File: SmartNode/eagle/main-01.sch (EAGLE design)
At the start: 151 parts, among them IC1 ATmega328P-AU, IC2 MAX3468CSA, IC4 78L33, IC5 MCP23017-E/SO-SOIC28, IC6 TPS56X200, IC7 LTC1694, Q1 IRLML2502, X0 OPI-ZERO

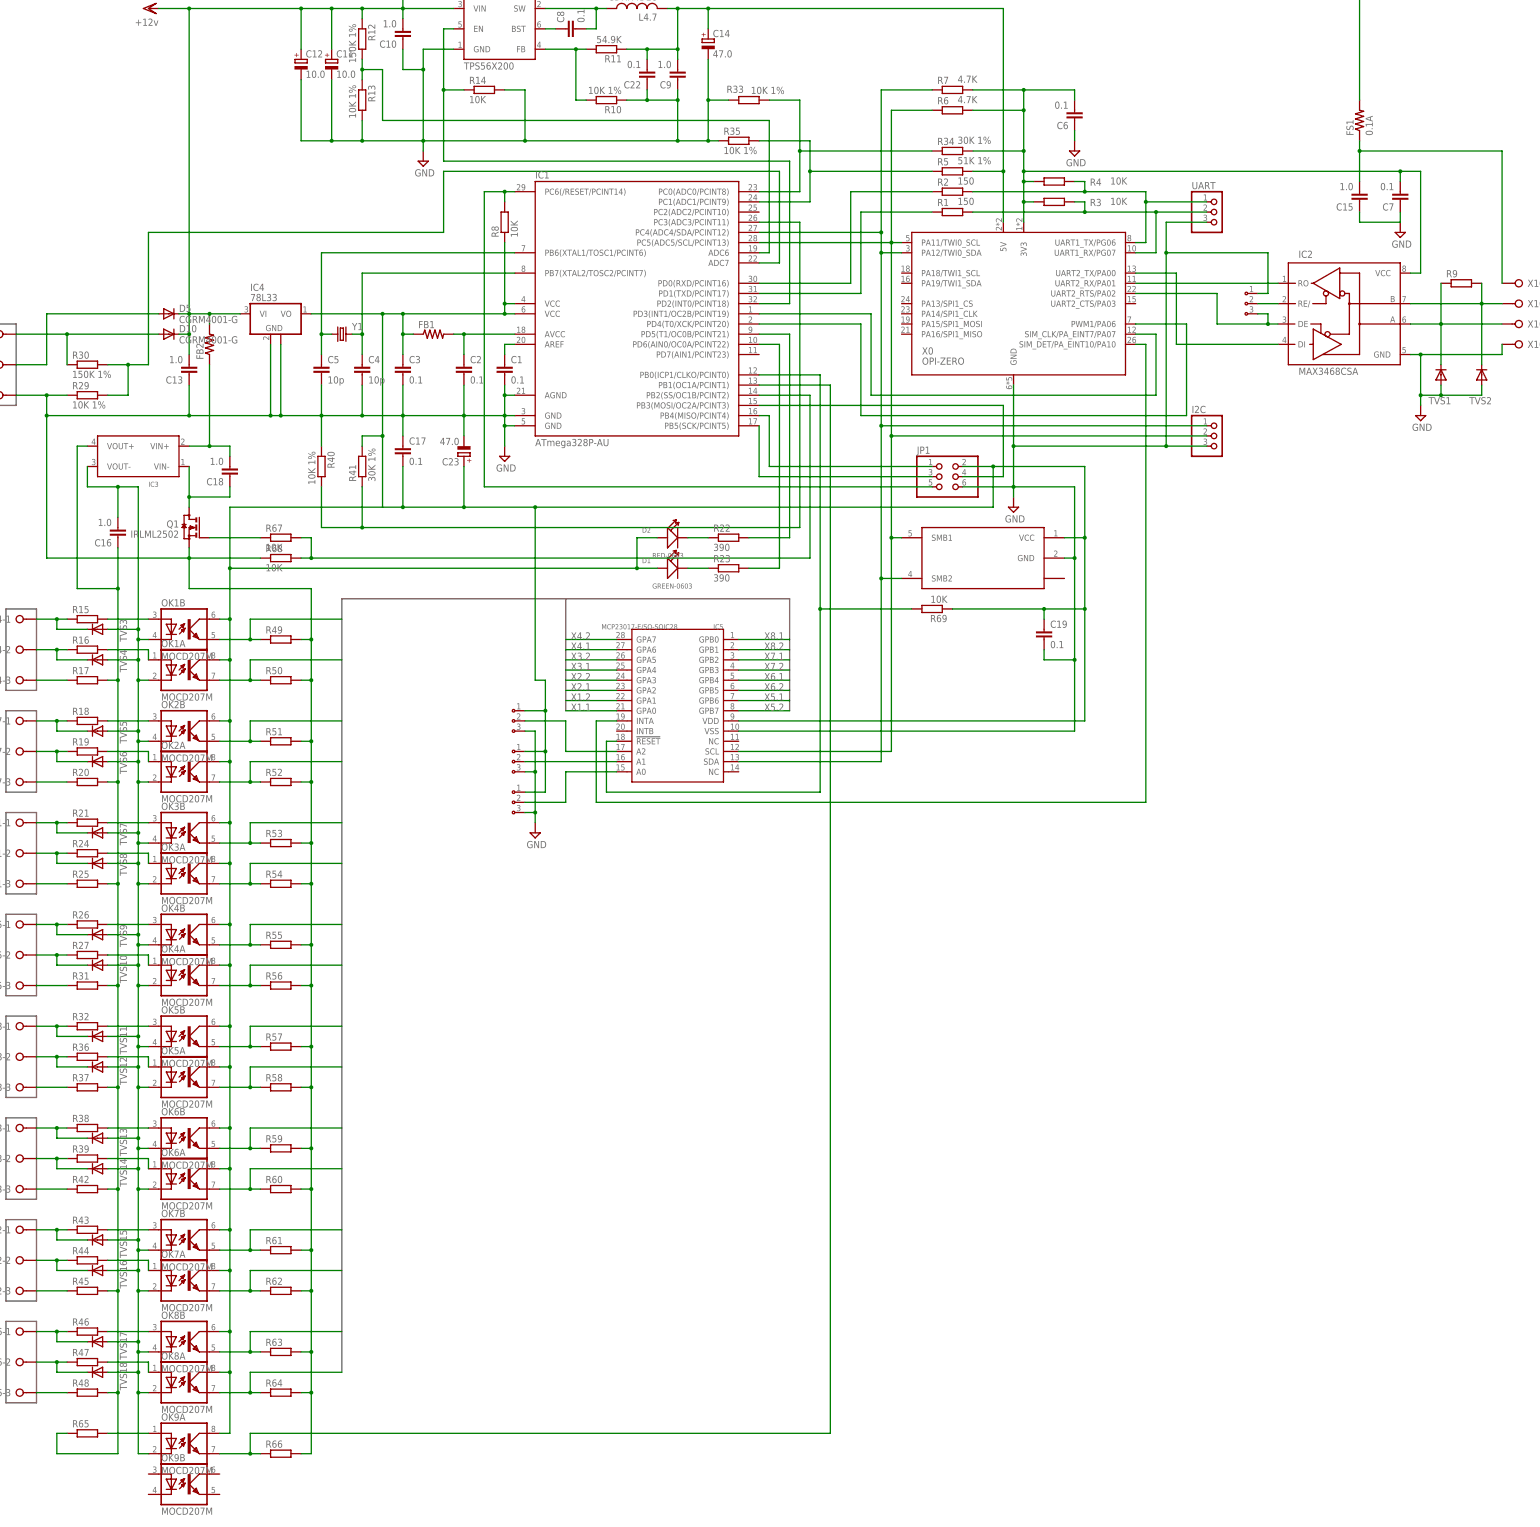
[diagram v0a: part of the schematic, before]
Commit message: Ann component values to schematic
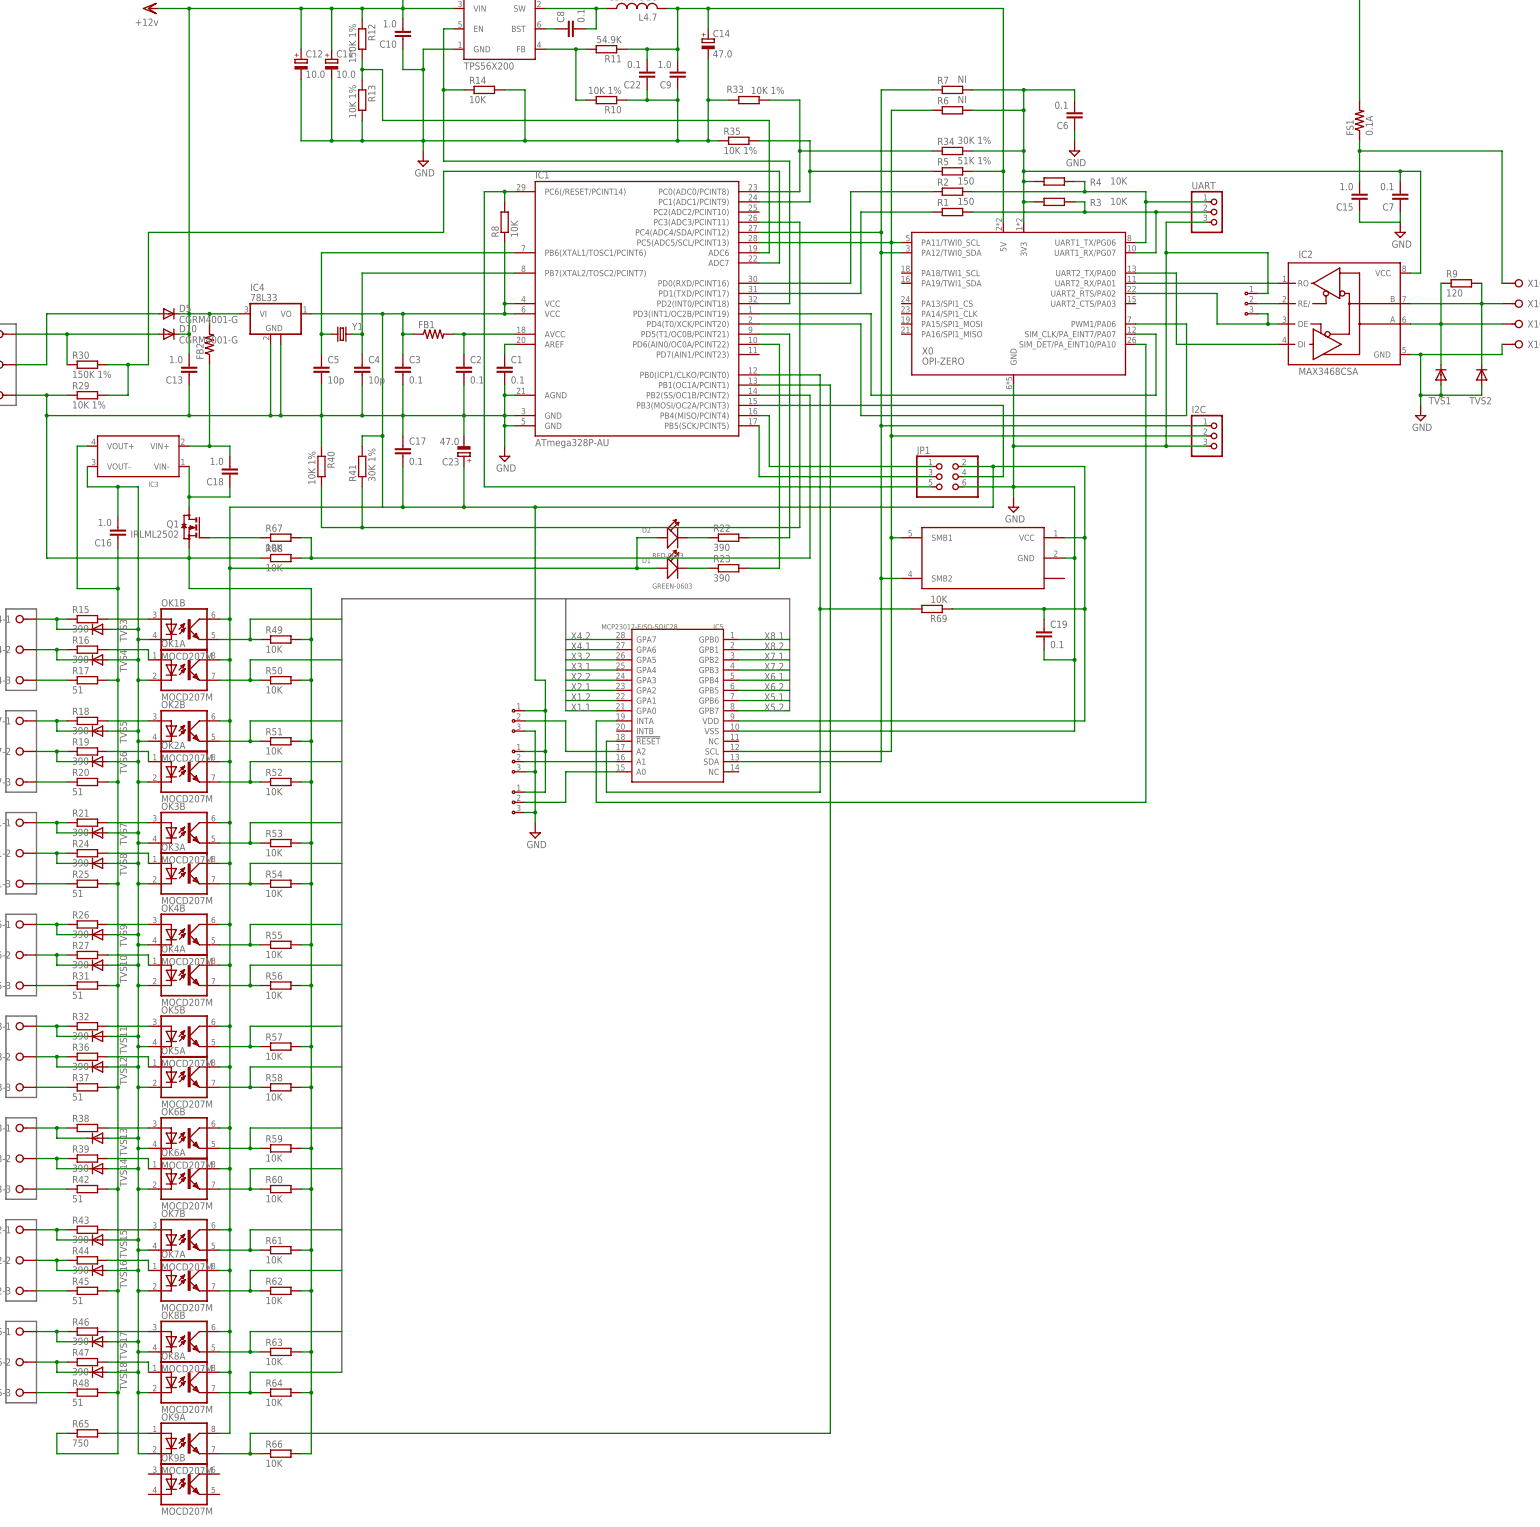
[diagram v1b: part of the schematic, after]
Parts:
- R15, R16, R18, R19, R21, R24, R26, R27, R32, R36, R39, R43, R44, R46, R47: value (none) -> 390
- R17, R20, R25, R31, R37, R42, R45, R48: value (none) -> 51
- R49, R50, R51, R52, R53, R54, R55, R56, R57, R58, R59, R60, R61, R62, R63, R64, R66: value (none) -> 10K
- R6, R7: value 4.7K -> NI
- R65: value (none) -> 750
- R9: value (none) -> 120
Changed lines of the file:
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@@
 <part name="R4" library="rcl" deviceset="R-EU_" device="R0603" value="10K"/>
 <part name="R5" library="rcl" deviceset="R-EU_" device="R0603" value="51K 1%"/>
-<part name="R6" library="rcl" deviceset="R-EU_" device="R0603" value="4.7K"/>
-<part name="R7" library="rcl" deviceset="R-EU_" device="R0603" value="4.7K"/>
+<part name="R6" library="rcl" deviceset="R-EU_" device="R0603" value="NI"/>
+<part name="R7" library="rcl" deviceset="R-EU_" device="R0603" value="NI"/>
 <part name="JP1" library="pinhead" deviceset="PINHD-2X3" device=""/>
 <part name="R8" library="rcl" deviceset="R-EU_" device="R0603" value="10K"/>
@@
 <part name="FS1" library="rcl" deviceset="R-US_" device="R1210" value="0.1A"/>
 <part name="C15" library="rcl" deviceset="C-EU" device="C1206" value="1.0"/>
-<part name="R9" library="rcl" deviceset="R-EU_" device="R1206"/>
+<part name="R9" library="rcl" deviceset="R-EU_" device="R1206" value="120"/>
 <part name="TVS1" library="diode" deviceset="DIODE-" device="SOD323-W"/>
 <part name="TVS2" library="diode" deviceset="DIODE-" device="SOD323-W"/>
@@
 <part name="OK7" library="optocoupler" deviceset="MOCD20*M" device="" technology="7"/>
 <part name="OK8" library="optocoupler" deviceset="MOCD20*M" device="" technology="7"/>
-<part name="R15" library="rcl" deviceset="R-EU_" device="R0603"/>
-<part name="R16" library="rcl" deviceset="R-EU_" device="R0603"/>
-<part name="R17" library="rcl" deviceset="R-EU_" device="R0603"/>
-<part name="R18" library="rcl" deviceset="R-EU_" device="R0603"/>
-<part name="R19" library="rcl" deviceset="R-EU_" device="R0603"/>
-<part name="R20" library="rcl" deviceset="R-EU_" device="R0603"/>
-<part name="R21" library="rcl" deviceset="R-EU_" device="R0603"/>
-<part name="R24" library="rcl" deviceset="R-EU_" device="R0603"/>
-<part name="R25" library="rcl" deviceset="R-EU_" device="R0603"/>
-<part name="R26" library="rcl" deviceset="R-EU_" device="R0603"/>
-<part name="R27" library="rcl" deviceset="R-EU_" device="R0603"/>
-<part name="R31" library="rcl" deviceset="R-EU_" device="R0603"/>
-<part name="R32" library="rcl" deviceset="R-EU_" device="R0603"/>
-<part name="R36" library="rcl" deviceset="R-EU_" device="R0603"/>
-<part name="R37" library="rcl" deviceset="R-EU_" device="R0603"/>
+<part name="R15" library="rcl" deviceset="R-EU_" device="R0603" value="390"/>
+<part name="R16" library="rcl" deviceset="R-EU_" device="R0603" value="390"/>
+<part name="R17" library="rcl" deviceset="R-EU_" device="R0603" value="51"/>
+<part name="R18" library="rcl" deviceset="R-EU_" device="R0603" value="390"/>
+<part name="R19" library="rcl" deviceset="R-EU_" device="R0603" value="390"/>
+<part name="R20" library="rcl" deviceset="R-EU_" device="R0603" value="51"/>
+<part name="R21" library="rcl" deviceset="R-EU_" device="R0603" value="390"/>
+<part name="R24" library="rcl" deviceset="R-EU_" device="R0603" value="390"/>
+<part name="R25" library="rcl" deviceset="R-EU_" device="R0603" value="51"/>
+<part name="R26" library="rcl" deviceset="R-EU_" device="R0603" value="390"/>
+<part name="R27" library="rcl" deviceset="R-EU_" device="R0603" value="390"/>
+<part name="R31" library="rcl" deviceset="R-EU_" device="R0603" value="51"/>
+<part name="R32" library="rcl" deviceset="R-EU_" device="R0603" value="390"/>
+<part name="R36" library="rcl" deviceset="R-EU_" device="R0603" value="390"/>
+<part name="R37" library="rcl" deviceset="R-EU_" device="R0603" value="51"/>
 <part name="R38" library="rcl" deviceset="R-EU_" device="R0603"/>
-<part name="R39" library="rcl" deviceset="R-EU_" device="R0603"/>
-<part name="R42" library="rcl" deviceset="R-EU_" device="R0603"/>
-<part name="R43" library="rcl" deviceset="R-EU_" device="R0603"/>
-<part name="R44" library="rcl" deviceset="R-EU_" device="R0603"/>
-<part name="R45" library="rcl" deviceset="R-EU_" device="R0603"/>
-<part name="R46" library="rcl" deviceset="R-EU_" device="R0603"/>
-<part name="R47" library="rcl" deviceset="R-EU_" device="R0603"/>
-<part name="R48" library="rcl" deviceset="R-EU_" device="R0603"/>
-<part name="R49" library="rcl" deviceset="R-EU_" device="R0603"/>
-<part name="R50" library="rcl" deviceset="R-EU_" device="R0603"/>
-<part name="R51" library="rcl" deviceset="R-EU_" device="R0603"/>
-<part name="R52" library="rcl" deviceset="R-EU_" device="R0603"/>
-<part name="R53" library="rcl" deviceset="R-EU_" device="R0603"/>
-<part name="R54" library="rcl" deviceset="R-EU_" device="R0603"/>
-<part name="R55" library="rcl" deviceset="R-EU_" device="R0603"/>
-<part name="R56" library="rcl" deviceset="R-EU_" device="R0603"/>
-<part name="R57" library="rcl" deviceset="R-EU_" device="R0603"/>
-<part name="R58" library="rcl" deviceset="R-EU_" device="R0603"/>
-<part name="R59" library="rcl" deviceset="R-EU_" device="R0603"/>
-<part name="R60" library="rcl" deviceset="R-EU_" device="R0603"/>
-<part name="R61" library="rcl" deviceset="R-EU_" device="R0603"/>
-<part name="R62" library="rcl" deviceset="R-EU_" device="R0603"/>
-<part name="R63" library="rcl" deviceset="R-EU_" device="R0603"/>
-<part name="R64" library="rcl" deviceset="R-EU_" device="R0603"/>
+<part name="R39" library="rcl" deviceset="R-EU_" device="R0603" value="390"/>
+<part name="R42" library="rcl" deviceset="R-EU_" device="R0603" value="51"/>
+<part name="R43" library="rcl" deviceset="R-EU_" device="R0603" value="390"/>
+<part name="R44" library="rcl" deviceset="R-EU_" device="R0603" value="390"/>
+<part name="R45" library="rcl" deviceset="R-EU_" device="R0603" value="51"/>
+<part name="R46" library="rcl" deviceset="R-EU_" device="R0603" value="390"/>
+<part name="R47" library="rcl" deviceset="R-EU_" device="R0603" value="390"/>
+<part name="R48" library="rcl" deviceset="R-EU_" device="R0603" value="51"/>
+<part name="R49" library="rcl" deviceset="R-EU_" device="R0603" value="10K"/>
+<part name="R50" library="rcl" deviceset="R-EU_" device="R0603" value="10K"/>
+<part name="R51" library="rcl" deviceset="R-EU_" device="R0603" value="10K"/>
+<part name="R52" library="rcl" deviceset="R-EU_" device="R0603" value="10K"/>
+<part name="R53" library="rcl" deviceset="R-EU_" device="R0603" value="10K"/>
+<part name="R54" library="rcl" deviceset="R-EU_" device="R0603" value="10K"/>
+<part name="R55" library="rcl" deviceset="R-EU_" device="R0603" value="10K"/>
+<part name="R56" library="rcl" deviceset="R-EU_" device="R0603" value="10K"/>
+<part name="R57" library="rcl" deviceset="R-EU_" device="R0603" value="10K"/>
+<part name="R58" library="rcl" deviceset="R-EU_" device="R0603" value="10K"/>
+<part name="R59" library="rcl" deviceset="R-EU_" device="R0603" value="10K"/>
+<part name="R60" library="rcl" deviceset="R-EU_" device="R0603" value="10K"/>
+<part name="R61" library="rcl" deviceset="R-EU_" device="R0603" value="10K"/>
+<part name="R62" library="rcl" deviceset="R-EU_" device="R0603" value="10K"/>
+<part name="R63" library="rcl" deviceset="R-EU_" device="R0603" value="10K"/>
+<part name="R64" library="rcl" deviceset="R-EU_" device="R0603" value="10K"/>
 <part name="OK9" library="optocoupler" deviceset="MOCD20*M" device="" technology="7"/>
-<part name="R65" library="rcl" deviceset="R-EU_" device="R0603"/>
-<part name="R66" library="rcl" deviceset="R-EU_" device="R0603"/>
+<part name="R65" library="rcl" deviceset="R-EU_" device="R0603" value="750"/>
+<part name="R66" library="rcl" deviceset="R-EU_" device="R0603" value="10K"/>
 <part name="C16" library="rcl" deviceset="C-EU" device="C1206" value="1.0"/>
 <part name="IC5" library="Seeed-OPL-ic" deviceset="INTERFACE-MCP23017-E(SOIC28)" device="" value="MCP23017-E/SO-SOIC28"/>
